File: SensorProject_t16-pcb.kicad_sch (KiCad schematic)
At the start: 60 parts, among them J1 Conn_01x02_Pin, J10 Conn_01x02_Pin, J11 Conn_01x02_Pin, J12 Conn_01x02_Pin, J13 Conn_01x02_Pin, J14 Conn_01x02_Pin, J15 Conn_01x02_Pin, J16 Conn_01x02_Pin, J17 Conn_01x04_Pin, J18 PinSocket_1x20_P2.54mm_Vertic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, J19 PinSocket_1x20_P2.54mm_Vertic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, J2 Conn_01x02_Pin, J20 Screw_Terminal_01x02, J3 Conn_01x02_Pin, J4 Conn_01x02_Pin, J5 Conn_01x02_Pin, J6 Conn_01x02_Pin, J7 Conn_01x02_Pin, J8 Conn_01x02_Pin, J9 Conn_01x02_Pin, U1 ADS1115IDGS, U2 ADS1115IDGS, U3 ADS1115IDGS, U4 ADS1115IDGS

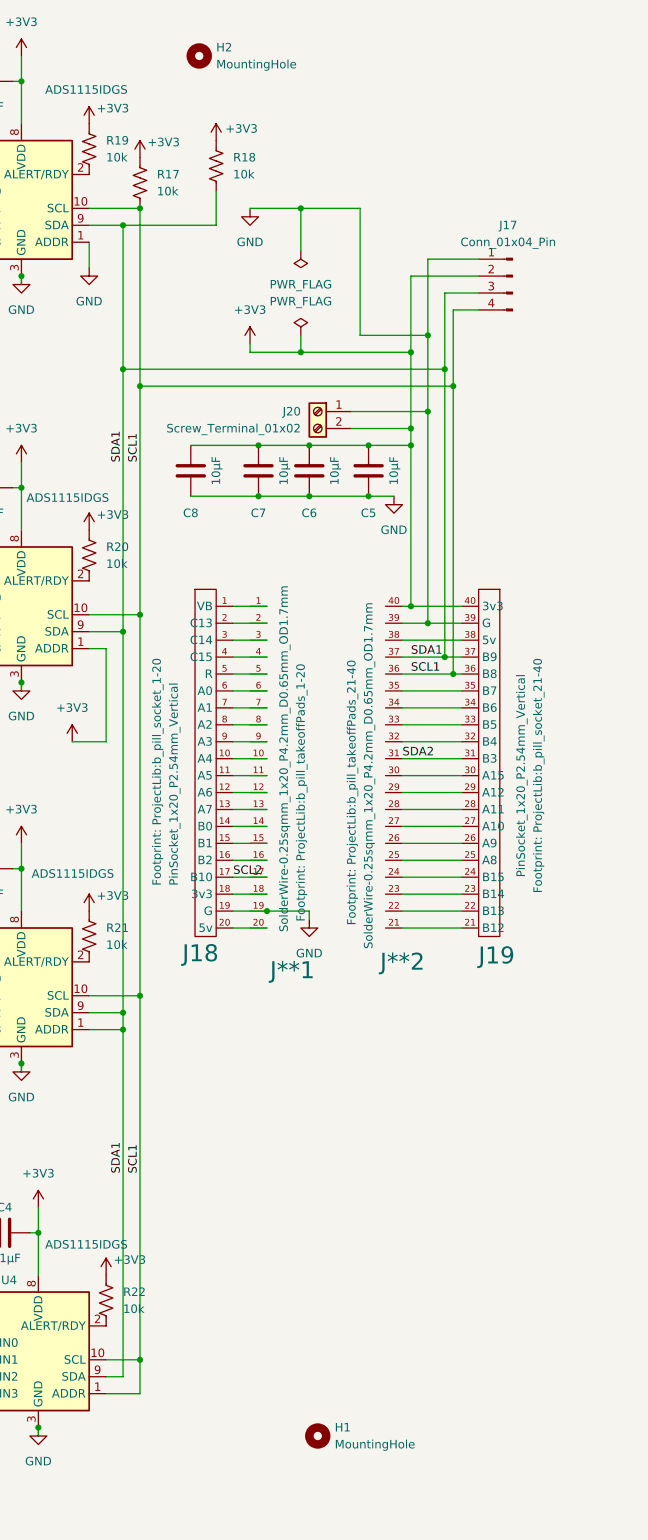
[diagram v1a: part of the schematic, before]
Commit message: adding sheets for power, radio, and f401.
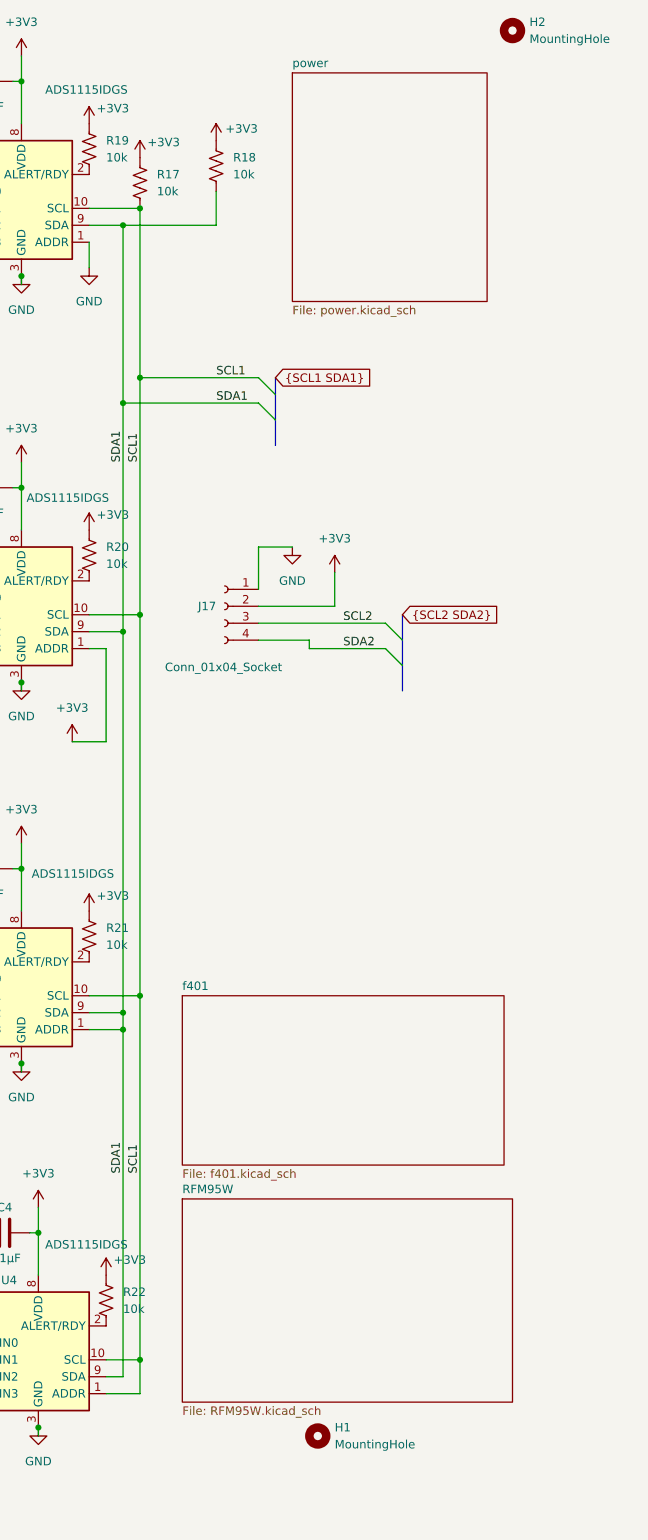
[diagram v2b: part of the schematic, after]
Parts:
- removed C5, C6, C7, C8: 10µF, ProjectLib:C_0805_2012Metric, symbol ProjectLib:C
- removed J**1: SolderWire-0.25sqmm_1x20_P4.2mm_D0.65mm_OD1.7mm, ProjectLib:b_pill_takeoffPads_1-20, symbol ProjectLib:b_pill_takeoff_1-20
- removed J**2: SolderWire-0.25sqmm_1x20_P4.2mm_D0.65mm_OD1.7mm, ProjectLib:b_pill_takeoffPads_21-40, symbol ProjectLib:b_pill_takeoff_21-40
- removed J17: Conn_01x04_Pin, ProjectLib:JST_XH_B4B-XH-A_1x04_P2.50mm_Vertical, symbol ProjectLib:Conn_01x04_Pin
- removed J18: PinSocket_1x20_P2.54mm_Vertical, ProjectLib:b_pill_socket_1-20, symbol ProjectLib:b_pill_1-20
- removed J19: PinSocket_1x20_P2.54mm_Vertical, ProjectLib:b_pill_socket_21-40, symbol ProjectLib:b_pill_21-40
- removed J20: Screw_Terminal_01x02, ProjectLib:TerminalBlock_Phoenix_MPT-0,5-2-2.54_1x02_P2.54mm_Horizontal, symbol ProjectLib:Screw_Terminal_01x02
- added J17: Conn_01x04_Socket, symbol Connector:Conn_01x04_Socket
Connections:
- net +3V3: now also J17.2 (Pin_2)
- net GND: now also J17.1 (Pin_1)
- net SCL2: now also J17.3 (Pin_3)
- net SDA2: now also J17.4 (Pin_4)
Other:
- added sheet RFM95W (RFM95W.kicad_sch)
- added sheet f401 (f401.kicad_sch)
- added sheet power (power.kicad_sch)
- moved on the sheet: H2

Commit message: ongoing add MCU and radio.
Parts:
- C1, C2, C3, C4: MountType (none) -> SMT
- J1, J10, J11, J12, J13, J14, J15, J16, J2, J3, J4, J5, J6, J7, J8, J9: MountType (none) -> PTH
- J17: footprint (none) -> ProjectLib:PinSocket_1x04_P2.54mm_Vertical; symbol Connector:Conn_01x04_Socket -> ProjectLib:Conn_01x04_Socket; MountType (none) -> PTH
- R1, R10, R11, R12, R13, R14, R15, R16, R17, R18, R19, R2, R20, R21, R22, R3, R4, R5, R6, R7, R8, R9: value 10k -> 10k 1%; MountType (none) -> SMT
- U1, U2, U3, U4: footprint ProjectLib:TSSOP-10_3x3mm_P0.5mm -> ProjectLib::TSSOP-10_3x3mm_P0.5mm; Manufacturer (none) -> TI; MfgPart (none) -> ADS1115IDGS; MountType (none) -> SMT

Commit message: f401.kicad_sch mostly complete other than xtals. Considering switch to f411 for memory, FPU, and generation 2 oscillator that gives better crystal choices.
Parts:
- R1, R10, R11, R12, R13, R14, R15, R16, R17, R18, R19, R2, R20, R21, R22, R3, R4, R5, R6, R7, R8, R9: footprint ProjectLib:R_0603_1608Metric -> ProjectLib:R_0201_0603Metric
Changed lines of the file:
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@@
 			)
 		)
-		(property "Footprint" "ProjectLib:R_0603_1608Metric"
+		(property "Footprint" "ProjectLib:R_0201_0603Metric"
 			(at 136.906 95.504 90)
 			(effects
@@
 			)
 		)
-		(property "Footprint" "ProjectLib:R_0603_1608Metric"
+		(property "Footprint" "ProjectLib:R_0201_0603Metric"
 			(at 144.526 39.624 90)
 			(effects
@@
 			)
 		)
-		(property "Footprint" "ProjectLib:R_0603_1608Metric"
+		(property "Footprint" "ProjectLib:R_0201_0603Metric"
 			(at 136.906 152.654 90)
 			(effects
@@
 			)
 		)
-		(property "Footprint" "ProjectLib:R_0603_1608Metric"
+		(property "Footprint" "ProjectLib:R_0201_0603Metric"
 			(at 82.296 197.104 90)
 			(effects
@@
 			)
 		)
-		(property "Footprint" "ProjectLib:R_0603_1608Metric"
+		(property "Footprint" "ProjectLib:R_0201_0603Metric"
 			(at 49.276 153.924 90)
 			(effects
@@
 			)
 		)
-		(property "Footprint" "ProjectLib:R_0603_1608Metric"
+		(property "Footprint" "ProjectLib:R_0201_0603Metric"
 			(at 79.756 51.054 90)
 			(effects
@@
 			)
 		)
-		(property "Footprint" "ProjectLib:R_0603_1608Metric"
+		(property "Footprint" "ProjectLib:R_0201_0603Metric"
 			(at 139.446 207.264 90)
 			(effects
@@
 			)
 		)
-		(property "Footprint" "ProjectLib:R_0603_1608Metric"
+		(property "Footprint" "ProjectLib:R_0201_0603Metric"
 			(at 82.296 223.774 90)
 			(effects
@@
 			)
 		)
-		(property "Footprint" "ProjectLib:R_0603_1608Metric"
+		(property "Footprint" "ProjectLib:R_0201_0603Metric"
 			(at 79.756 112.014 90)
 			(effects
@@
 			)
 		)
-		(property "Footprint" "ProjectLib:R_0603_1608Metric"
+		(property "Footprint" "ProjectLib:R_0201_0603Metric"
 			(at 79.756 145.034 90)
 			(effects
@@
 			)
 		)
-		(property "Footprint" "ProjectLib:R_0603_1608Metric"
+		(property "Footprint" "ProjectLib:R_0201_0603Metric"
 			(at 136.906 34.544 90)
 			(effects
@@
 			)
 		)
-		(property "Footprint" "ProjectLib:R_0603_1608Metric"
+		(property "Footprint" "ProjectLib:R_0201_0603Metric"
 			(at 49.276 62.484 90)
 			(effects
@@
 			)
 		)
-		(property "Footprint" "ProjectLib:R_0603_1608Metric"
+		(property "Footprint" "ProjectLib:R_0201_0603Metric"
 			(at 49.276 35.814 90)
 			(effects
@@
 			)
 		)
-		(property "Footprint" "ProjectLib:R_0603_1608Metric"
+		(property "Footprint" "ProjectLib:R_0201_0603Metric"
 			(at 79.756 24.384 90)
 			(effects
@@
 			)
 		)
-		(property "Footprint" "ProjectLib:R_0603_1608Metric"
+		(property "Footprint" "ProjectLib:R_0201_0603Metric"
 			(at 50.546 123.444 90)
 			(effects
@@
 			)
 		)
-		(property "Footprint" "ProjectLib:R_0603_1608Metric"
+		(property "Footprint" "ProjectLib:R_0201_0603Metric"
 			(at 50.546 211.074 90)
 			(effects
@@
 			)
 		)
-		(property "Footprint" "ProjectLib:R_0603_1608Metric"
+		(property "Footprint" "ProjectLib:R_0201_0603Metric"
 			(at 50.546 246.634 90)
 			(effects
@@
 			)
 		)
-		(property "Footprint" "ProjectLib:R_0603_1608Metric"
+		(property "Footprint" "ProjectLib:R_0201_0603Metric"
 			(at 51.816 96.774 90)
 			(effects
@@
 			)
 		)
-		(property "Footprint" "ProjectLib:R_0603_1608Metric"
+		(property "Footprint" "ProjectLib:R_0201_0603Metric"
 			(at 49.276 180.594 90)
 			(effects
@@
 			)
 		)
-		(property "Footprint" "ProjectLib:R_0603_1608Metric"
+		(property "Footprint" "ProjectLib:R_0201_0603Metric"
 			(at 82.296 169.164 90)
 			(effects
@@
 			)
 		)
-		(property "Footprint" "ProjectLib:R_0603_1608Metric"
+		(property "Footprint" "ProjectLib:R_0201_0603Metric"
 			(at 79.756 85.344 90)
 			(effects
@@
 			)
 		)
-		(property "Footprint" "ProjectLib:R_0603_1608Metric"
+		(property "Footprint" "ProjectLib:R_0201_0603Metric"
 			(at 155.956 37.084 90)
 			(effects

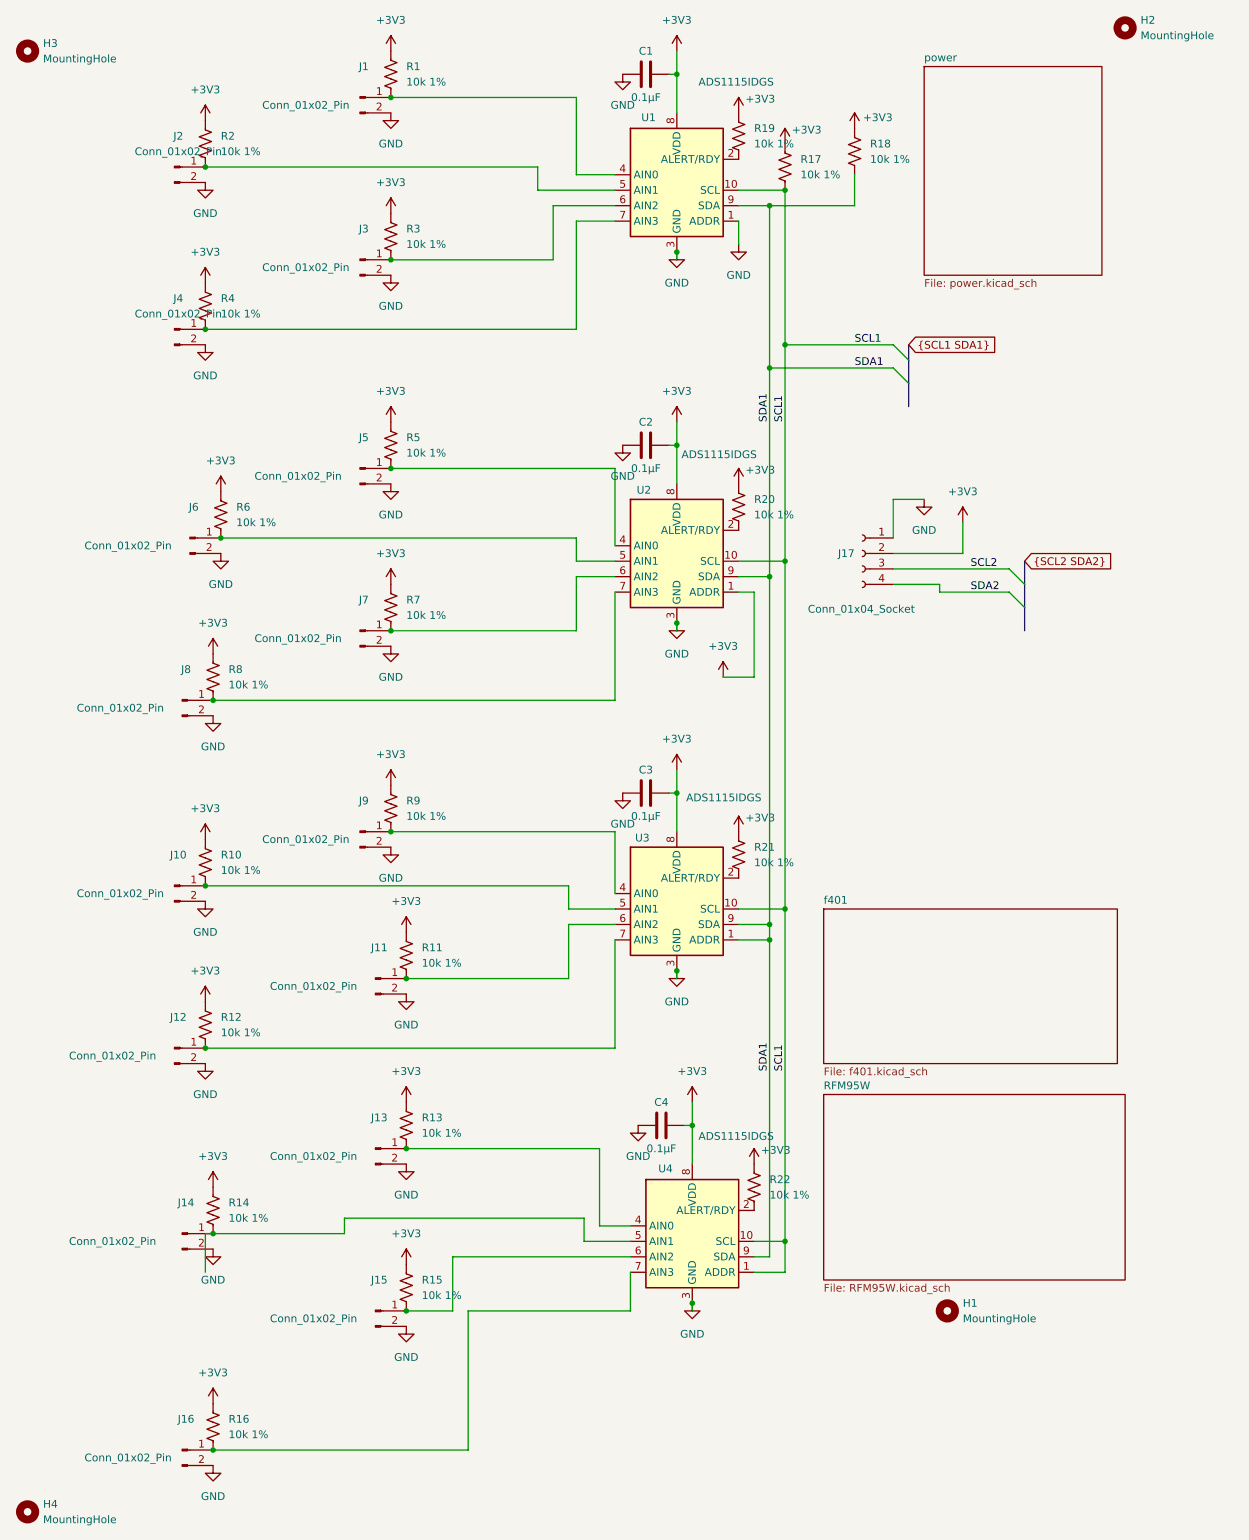
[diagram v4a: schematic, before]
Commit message: switched to F411. Added sheets for LSE and HSE.
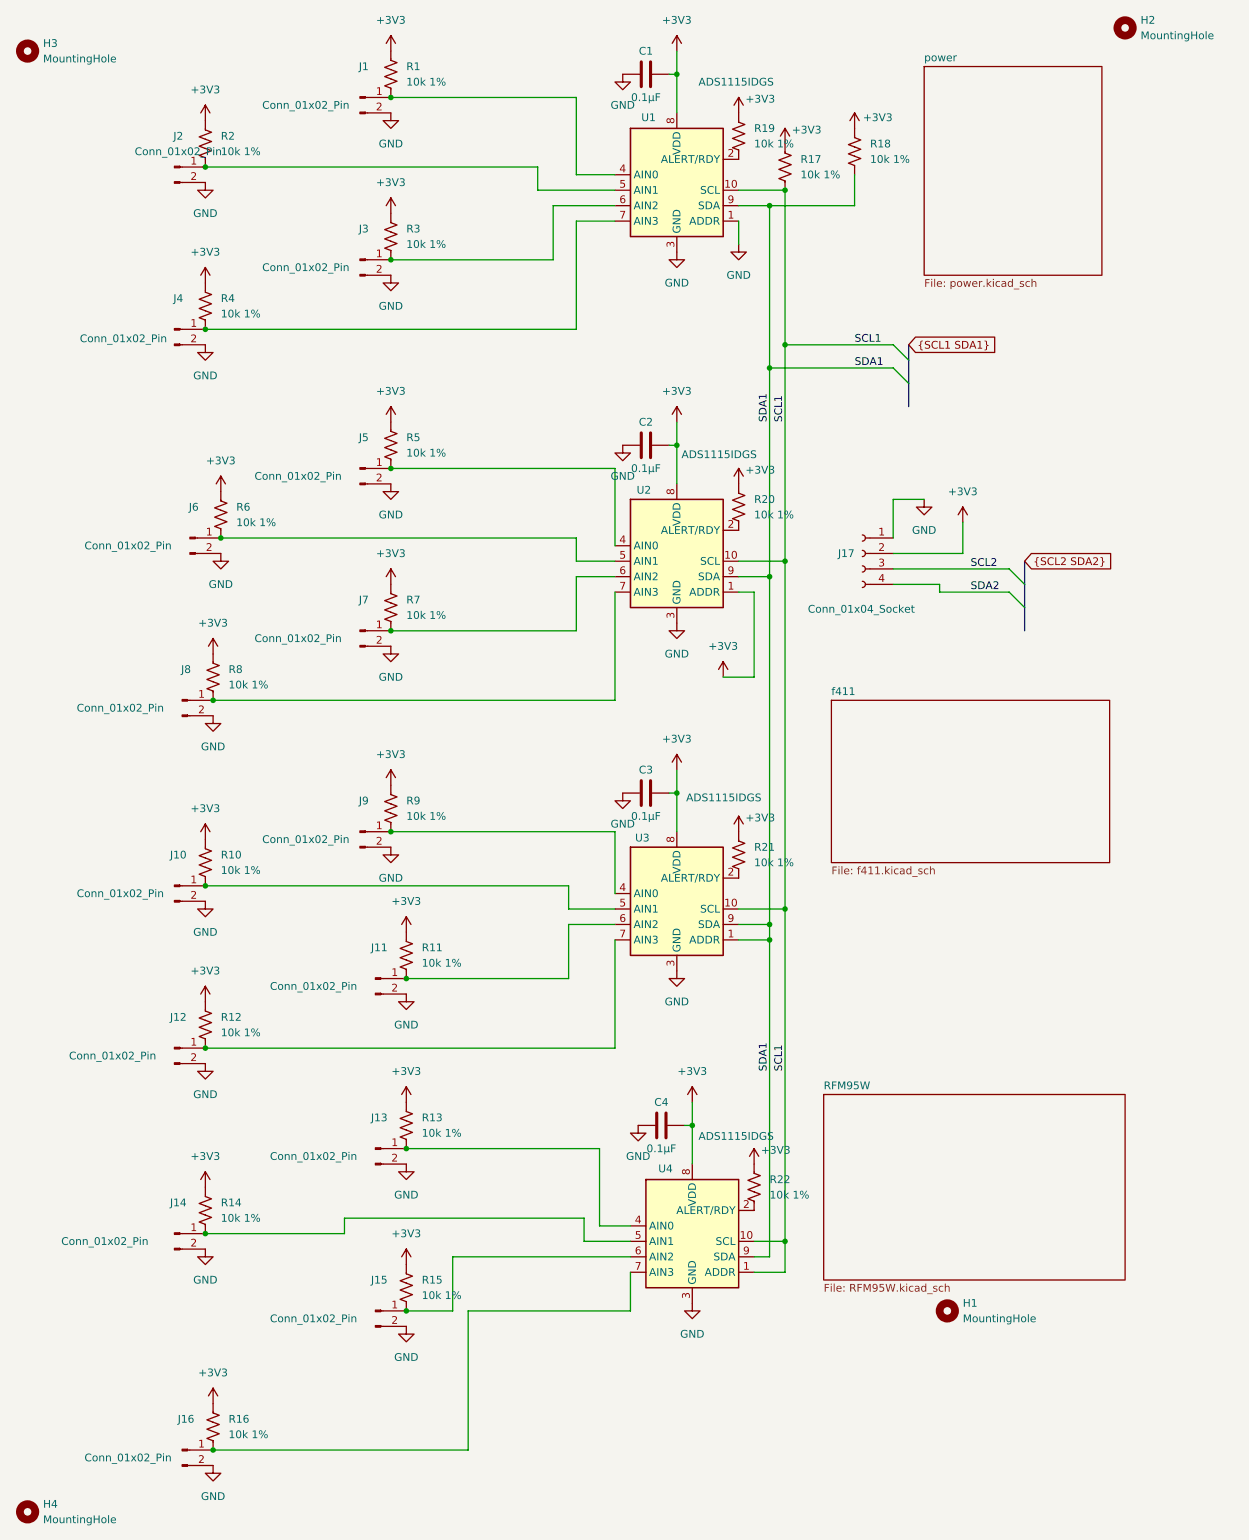
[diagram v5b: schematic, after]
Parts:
- R1, R10, R11, R12, R13, R14, R15, R16, R17, R18, R19, R2, R20, R21, R22, R3, R4, R5, R6, R7, R8, R9: footprint ProjectLib:R_0201_0603Metric -> ProjectLib:R_0603_1608Metric
- U1, U2, U3, U4: footprint ProjectLib::TSSOP-10_3x3mm_P0.5mm -> ProjectLib:TSSOP-10_3x3mm_P0.5mm
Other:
- removed sheet f401
- added sheet f411 (f411.kicad_sch)
- moved on the sheet: J14, R14
